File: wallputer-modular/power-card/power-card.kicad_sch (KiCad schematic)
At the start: 1 part

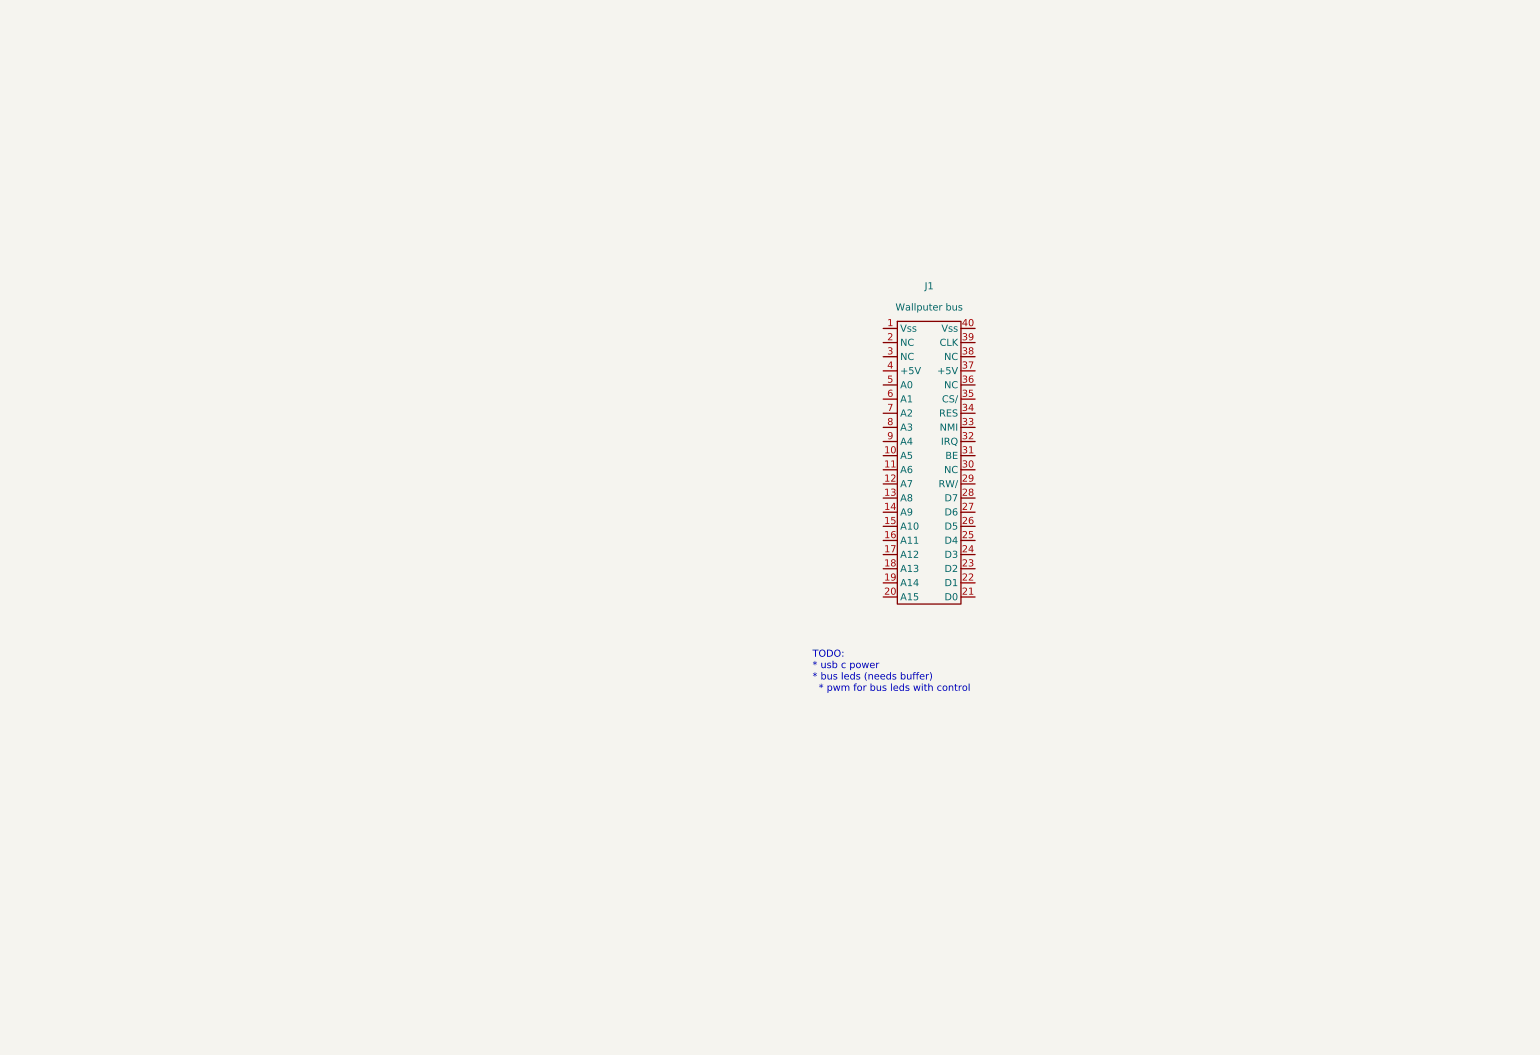
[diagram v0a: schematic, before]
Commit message: implement power module
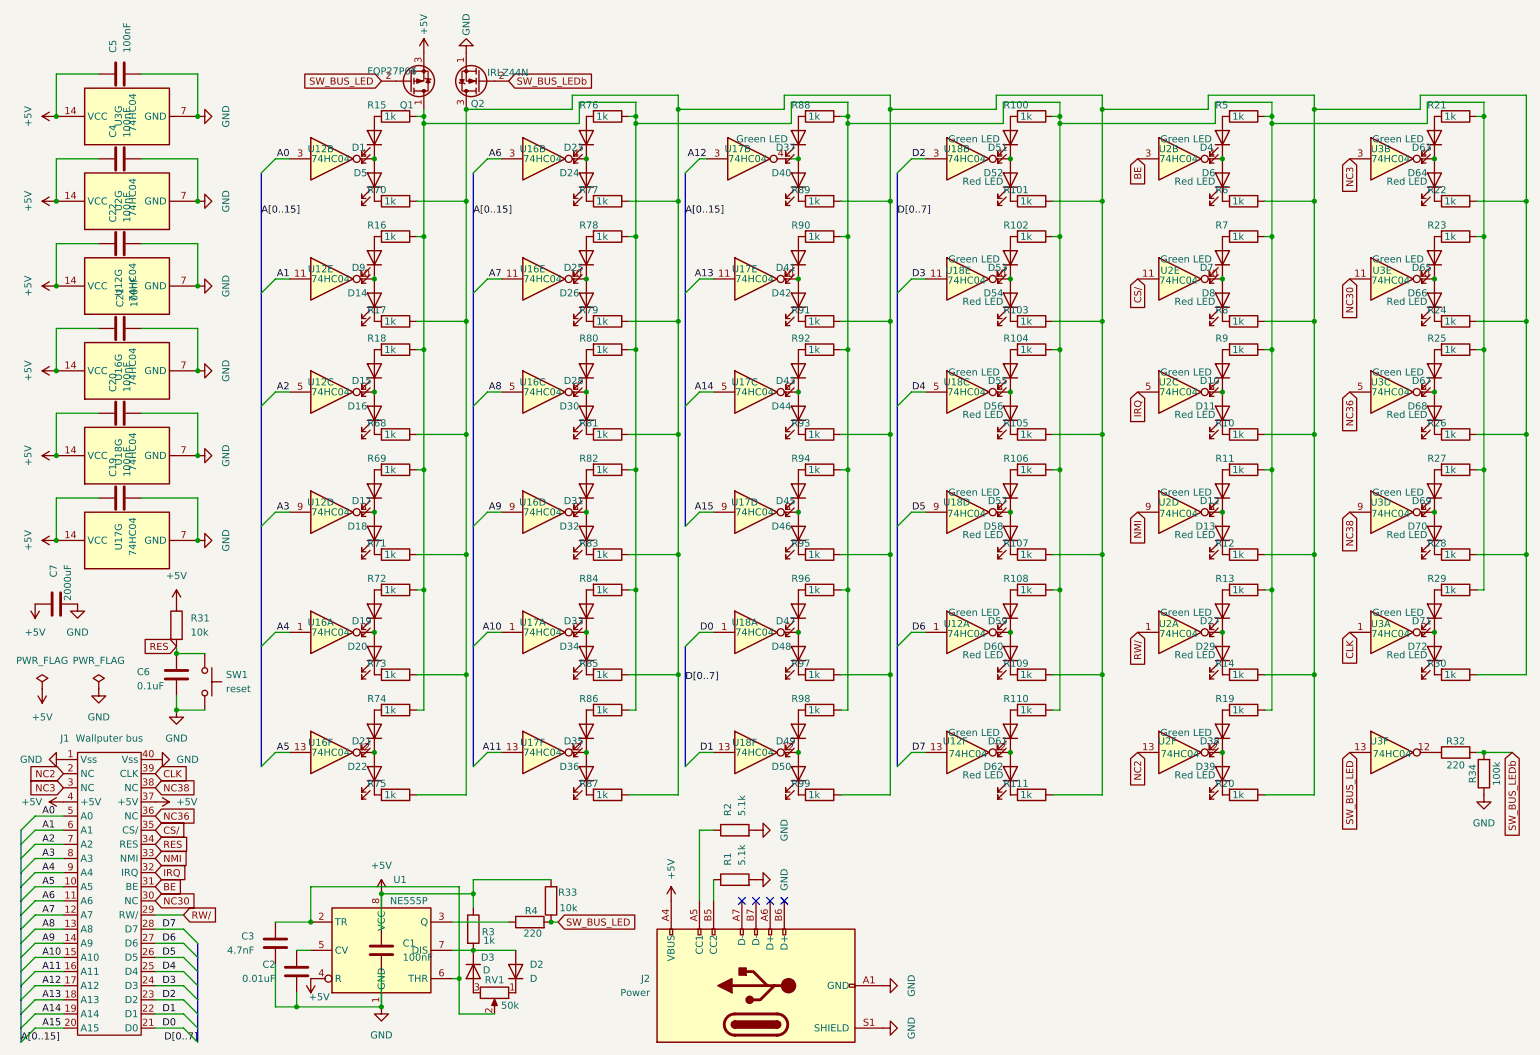
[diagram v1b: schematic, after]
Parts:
- added C1: 100nF, symbol Device:C
- added C19, C20, C21, C22, C4, C5: 100nF, Capacitor_THT:C_Disc_D5.0mm_W2.5mm_P5.00mm, symbol Device:C
- added C2: 0.01uF, symbol Device:C
- added C3: 4.7nF, symbol Device:C
- added C6: 0.1uF, symbol Device:C
- added C7: 2000uF, symbol Device:C
- added D1, D10, D12, D15, D17, D19, D21, D23, D25, D27, D28, D31, D33, D35, D37, D38, D4, D41, D43, D45, D47, D49, D51, D53, D55, D57, D59, D61, D63, D65, D67, D69, D7, D71, D9: Green LED, LED_THT:LED_D3.0mm, symbol Device:LED
- added D11, D13, D14, D16, D18, D20, D22, D24, D26, D29, D30, D32, D34, D36, D39, D40, D42, D44, D46, D48, D5, D50, D52, D54, D56, D58, D6, D60, D62, D64, D66, D68, D70, D72, D8: Red LED, LED_THT:LED_D3.0mm, symbol Device:LED
- added D2, D3: D, symbol Device:D
- added J2: Power, symbol Connector:USB_C_Receptacle_USB2.0_14P
- added Q1: FQP27P06, Package_TO_SOT_THT:TO-92_Inline, symbol Transistor_FET:BS250
- added Q2: IRLZ44N, Package_TO_SOT_THT:TO-92_Inline, symbol Transistor_FET:2N7000
- added R1, R2: 5.1k, symbol Device:R
- added R10, R100, R101, R102, R103, R104, R105, R106, R107, R108, R109, R11, R110, R111, R12, R13, R14, R15, R16, R17, R18, R19, R20, R21, R22, R23, R24, R25, R26, R27, R28, R29, R30, R5, R6, R68, R69, R7, R70, R71, R72, R73, R74, R75, R76, R77, R78, R79, R8, R80, R81, R82, R83, R84, R85, R86, R87, R88, R89, R9, R90, R91, R92, R93, R94, R95, R96, R97, R98, R99: 1k, Resistor_THT:R_Axial_DIN0204_L3.6mm_D1.6mm_P2.54mm_Vertical, symbol Device:R
- added R3: 1k, symbol Device:R
- added R31, R33: 10k, symbol Device:R
- added R32, R4: 220, symbol Device:R
- added R34: 100k, symbol Device:R
- added RV1: 50k, symbol Device:R_Potentiometer
- added SW1: reset, symbol Switch:SW_Push
- added U1: NE555P, Package_DIP:DIP-8_W7.62mm, symbol Timer:NE555P
- added U12, U16, U17, U18, U2, U3: 74HC04, Package_DIP:DIP-14_W7.62mm_Socket, symbol 74xx:74HC04
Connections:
- net GND: now reaches J1.1 (Vss)
- net GND: now also J1.40 (Vss), C1.2, C19.2, C2.1, C20.2, C21.2, C22.2, C3.2, C4.2, C5.2, C6.2, C7.2, J2.A1 (GND), J2.A12 (GND), J2.B1 (GND), J2.B12 (GND), J2.S1 (SHIELD), Q2.1 (S), R1.2, R2.2, R34.1, SW1.2, U1.1 (GND), U12.7 (GND), U16.7 (GND), U17.7 (GND), U18.7 (GND), U2.7 (GND), U3.7 (GND)
- net A5: now reaches J1.10 (A5)
- net A5: now also U16.13
- net A6: now reaches J1.11 (A6)
- net A6: now also U16.3
- net A7: now reaches J1.12 (A7)
- net A7: now also U16.11
- net A8: now reaches J1.13 (A8)
- net A8: now also U16.5
- net A9: now reaches J1.14 (A9)
- net A9: now also U16.9
- net A10: now reaches J1.15 (A10)
- net A10: now also U17.1
- net A11: now reaches J1.16 (A11)
- net A11: now also U17.13
- net A12: now reaches J1.17 (A12)
- net A12: now also U17.3
- net A13: now reaches J1.18 (A13)
- net A13: now also U17.11
- net A14: now reaches J1.19 (A14)
- net A14: now also U17.5
- net NC2: now reaches J1.2 (NC)
- net NC2: now also U2.13
- net A15: now reaches J1.20 (A15)
- net A15: now also U17.9
- net D0: now reaches J1.21 (D0)
- net D0: now also U18.1
- net D1: now reaches J1.22 (D1)
- net D1: now also U18.13
- net D2: now reaches J1.23 (D2)
- net D2: now also U18.3
- net D3: now reaches J1.24 (D3)
- net D3: now also U18.11
- net D4: now reaches J1.25 (D4)
- net D4: now also U18.5
- net D5: now reaches J1.26 (D5)
- net D5: now also U18.9
- net D6: now reaches J1.27 (D6)
- net D6: now also U12.1
- net D7: now reaches J1.28 (D7)
- net D7: now also U12.13
- net RW/: now reaches J1.29 (RW/)
- net RW/: now also U2.1
- net NC3: now reaches J1.3 (NC)
- net NC3: now also U3.3
- net NC30: now reaches J1.30 (NC)
- net NC30: now also U3.11
- net BE: now reaches J1.31 (BE)
- net BE: now also U2.3
- net IRQ: now reaches J1.32 (IRQ)
- net IRQ: now also U2.5
- net NMI: now reaches J1.33 (NMI)
- net NMI: now also U2.9
- net RES: now reaches J1.34 (RES)
- net RES: now also C6.1, R31.2, SW1.1
- net CS/: now reaches J1.35 (CS/)
- net CS/: now also U2.11
- net NC36: now reaches J1.36 (NC)
- net NC36: now also U3.5
- net +5V: now reaches J1.37 (+5V)
- net +5V: now also J1.4 (+5V), C1.1, C19.1, C20.1, C21.1, C22.1, C4.1, C5.1, C7.1, J2.A4 (VBUS), J2.A9 (VBUS), J2.B4 (VBUS), J2.B9 (VBUS), Q1.3 (S), R3.1, R31.1, R33.2, U1.4 (R), U1.8 (VCC), U12.14 (VCC), U16.14 (VCC), U17.14 (VCC), U18.14 (VCC), U2.14 (VCC), U3.14 (VCC)
- net NC38: now reaches J1.38 (NC)
- net NC38: now also U3.9
- net CLK: now reaches J1.39 (CLK)
- net CLK: now also U3.1
- net A0: now reaches J1.5 (A0)
- net A0: now also U12.3
- net A1: now reaches J1.6 (A1)
- net A1: now also U12.11
- net A2: now reaches J1.7 (A2)
- net A2: now also U12.5
- net A3: now reaches J1.8 (A3)
- net A3: now also U12.9
- net A4: now reaches J1.9 (A4)
- net A4: now also U16.1
- new net: D26.1 (K), R79.2
- new net: D25.1 (K), D26.2 (A), U16.10
- new net: D35.1 (K), D36.2 (A), U17.12
- new net: J2.B5 (CC2), R1.1
- new net: C3.1, RV1.2, U1.2 (TR), U1.6 (THR)
- new net: D1.1 (K), D5.2 (A), U12.4
- new net: D14.2 (A), D9.1 (K), U12.10
- new net: D9.2 (A), R16.2
- new net: D63.1 (K), D64.2 (A), U3.4
- new net: D63.2 (A), R21.2
- new net: D8.1 (K), R8.2
- new net: D7.1 (K), D8.2 (A), U2.10
- new net: Q2.3 (D), R10.1, R101.1, R103.1, R105.1, R107.1, R109.1, R111.1, R12.1, R14.1, R17.1, R20.1, R22.1, R24.1, R26.1, R28.1, R30.1, R6.1, R68.1, R70.1, R71.1, R73.1, R75.1, R77.1, R79.1, R8.1, R81.1, R83.1, R85.1, R87.1, R89.1, R91.1, R93.1, R95.1, R97.1, R99.1
- new net: D62.1 (K), R111.2
- new net: D37.1 (K), D40.2 (A), U17.4
- new net: D64.1 (K), R22.2
- new net: Q1.1 (D), R100.1, R102.1, R104.1, R106.1, R108.1, R11.1, R110.1, R13.1, R15.1, R16.1, R18.1, R19.1, R21.1, R23.1, R25.1, R27.1, R29.1, R5.1, R69.1, R7.1, R72.1, R74.1, R76.1, R78.1, R80.1, R82.1, R84.1, R86.1, R88.1, R9.1, R90.1, R92.1, R94.1, R96.1, R98.1
- new net: D43.2 (A), R92.2
- new net: D16.1 (K), R68.2
- new net: D15.1 (K), D16.2 (A), U12.6
- new net: D49.2 (A), R98.2
- new net: D39.1 (K), R20.2
- new net: D38.1 (K), D39.2 (A), U2.12
- new net: J2.A5 (CC1), R2.1
- new net: D44.1 (K), R93.2
- new net: D43.1 (K), D44.2 (A), U17.6
- new net: D1.2 (A), R15.2
- new net: D33.2 (A), R84.2
- new net: D27.1 (K), D29.2 (A), U2.2
- new net: D47.1 (K), D48.2 (A), U18.2
- new net: D47.2 (A), R96.2
- new net: D41.1 (K), D42.2 (A), U17.10
- new net: D41.2 (A), R90.2
- new net: D24.1 (K), R77.2
- new net: D23.1 (K), D24.2 (A), U16.4
- new net: D56.1 (K), R105.2
- new net: D55.1 (K), D56.2 (A), U18.6
- new net: D23.2 (A), R76.2
- new net: D32.1 (K), R83.2
- new net: R32.1, U3.12
- new net: D27.2 (A), R13.2
- new net: D25.2 (A), R78.2
- new net: D31.1 (K), D32.2 (A), U16.8
- new net: D31.2 (A), R82.2
- new net: D22.1 (K), R75.2
- new net: D12.1 (K), D13.2 (A), U2.8
- new net: D12.2 (A), R11.2
- new net: D65.1 (K), D66.2 (A), U3.10
- new net: D65.2 (A), R23.2
- new net: D52.1 (K), R101.2
- new net: D51.1 (K), D52.2 (A), U18.4
- new net: D2.2 (A), D3.1 (K), R3.2, U1.7 (DIS)
- new net: D3.2 (A), RV1.3
- new net: D40.1 (K), R89.2
- new net: D46.1 (K), R95.2
- new net: D13.1 (K), R12.2
- new net: D18.1 (K), R71.2
- new net: D17.1 (K), D18.2 (A), U12.8
- new net: D60.1 (K), R109.2
- new net: D59.1 (K), D60.2 (A), U12.2
- new net: D53.1 (K), D54.2 (A), U18.10
- new net: D36.1 (K), R87.2
- new net: D21.2 (A), R74.2
- new net: D50.1 (K), R99.2
- new net: D49.1 (K), D50.2 (A), U18.12
- new net: D17.2 (A), R69.2
- new net: D42.1 (K), R91.2
- new net: D29.1 (K), R14.2
- new net: D28.1 (K), D30.2 (A), U16.6
- new net: D72.1 (K), R30.2
- new net: D71.1 (K), D72.2 (A), U3.2
- new net: D66.1 (K), R24.2
- new net: D21.1 (K), D22.2 (A), U16.12
- new net: D15.2 (A), R18.2
- new net: D5.1 (K), R70.2
- new net: D48.1 (K), R97.2
- new net: D51.2 (A), R100.2
- new net: D53.2 (A), R102.2
- new net: D34.1 (K), R85.2
- new net: D33.1 (K), D34.2 (A), U17.2
- new net: D10.1 (K), D11.2 (A), U2.6
- new net: D10.2 (A), R9.2
- new net: D38.2 (A), R19.2
- new net: D59.2 (A), R108.2
- new net: D57.1 (K), D58.2 (A), U18.8
- new net: D37.2 (A), R88.2
- new net: D20.1 (K), R73.2
- new net: D19.1 (K), D20.2 (A), U16.2
- new net: D30.1 (K), R81.2
- new net: D68.1 (K), R26.2
- new net: D45.1 (K), D46.2 (A), U17.8
- new net: D57.2 (A), R106.2
- new net: D61.1 (K), D62.2 (A), U12.12
- new net: D61.2 (A), R110.2
- new net: D71.2 (A), R29.2
- new net: D35.2 (A), R86.2
- new net: D14.1 (K), R17.2
- new net: D67.1 (K), D68.2 (A), U3.6
- new net: D67.2 (A), R25.2
- new net: C2.2, U1.5 (CV)
- new net: D6.1 (K), R6.2
- new net: D4.1 (K), D6.2 (A), U2.4
- new net: D69.1 (K), D70.2 (A), U3.8
- new net: D69.2 (A), R27.2
- new net: R4.1, U1.3 (Q)
- new net: D70.1 (K), R28.2
- new net: D4.2 (A), R5.2
- new net: D45.2 (A), R94.2
- new net: D58.1 (K), R107.2
- new net: D55.2 (A), R104.2
- new net: D28.2 (A), R80.2
- new net: D54.1 (K), R103.2
- new net: D2.1 (K), RV1.1
- new net: D7.2 (A), R7.2
- new net: D19.2 (A), R72.2
- new net: D11.1 (K), R10.2
- new net SW_BUS_LED: Q1.2 (G), R33.1, R4.2, U3.13
- new net SW_BUS_LEDb: Q2.2 (G), R32.2, R34.2
- no-connect marks 0 -> 4
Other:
- note removed: "TODO: * usb c power * bus leds (needs buffer) * pwm for bus leds with control"

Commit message: fix errors
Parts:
- removed C7: 2000uF, symbol Device:C
- added C7: 2000uF, Capacitor_THT:CP_Radial_D18.0mm_P7.50mm, symbol Device:C_Polarized
- Q1: footprint Package_TO_SOT_THT:TO-92_Inline -> Package_TO_SOT_THT:TO-220-3_Vertical; symbol Transistor_FET:BS250 -> Transistor_FET:FQP27P06
- Q2: footprint Package_TO_SOT_THT:TO-92_Inline -> Package_TO_SOT_THT:TO-220-3_Vertical; symbol Transistor_FET:2N7000 -> Transistor_FET:IRLZ44N
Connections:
- net +5V: now also C7.1
- net GND: now also Q2.3 (S), C7.2; no longer Q2.1 (S)
- net SW_BUS_LED: now also Q1.1 (G); no longer Q1.2 (G)
- net SW_BUS_LEDb: now also Q2.1 (G); no longer Q2.2 (G)
- net at R10.1, R101.1, R103.1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: now also Q2.2 (D); no longer Q2.3 (D)
- net at R100.1, R102.1, R104.1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: now also Q1.2 (D); no longer Q1.1 (D)
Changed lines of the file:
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@@
 	)
 	(symbol
-		(lib_id "Transistor_FET:BS250")
+		(lib_id "Transistor_FET:FQP27P06")
 		(at 82.55 24.13 0)
 		(mirror x)
@@
 			)
 		)
-		(property "Footprint" "Package_TO_SOT_THT:TO-92_Inline"
+		(property "Footprint" "Package_TO_SOT_THT:TO-220-3_Vertical"
 			(at 87.63 22.225 0)
 			(effects
@@
 			)
 		)
-		(property "Datasheet" "http://www.vishay.com/docs/70209/70209.pdf"
+		(property "Datasheet" "https://www.onsemi.com/pub/Collateral/FQP27P06-D.PDF"
 			(at 87.63 20.32 0)
 			(effects
@@
 			)
 		)
-		(property "Description" "-0.18A Id, -45V Vds, P-Channel MOSFET, TO-92"
+		(property "Description" "-27A Id, -60V Vds, QFET P-Channel MOSFET, TO-220"
 			(at 82.55 24.13 0)
 			(effects
@@
 	)
 	(symbol
-		(lib_id "Device:C")
-		(at 19.05 118.11 90)
-		(mirror x)
-		(unit 1)
-		(exclude_from_sim no)
-		(in_bom yes)
-		(on_board yes)
-		(dnp no)
-		(property "Reference" "C7"
-			(at 18.542 110.998 0)
-			(effects
-				(font
-					(size 1.27 1.27)
-				)
-				(justify left)
-			)
-		)
-		(property "Value" "2000uF"
-			(at 21.082 110.998 0)
-			(effects
-				(font
-					(size 1.27 1.27)
-				)
-				(justify left)
-			)
-		)
-		(property "Footprint" ""
-			(at 22.86 119.0752 0)
-			(effects
-				(font
-					(size 1.27 1.27)
-				)
-				(hide yes)
-			)
-		)
-		(property "Datasheet" "~"
-			(at 19.05 118.11 0)
-			(effects
-				(font
-					(size 1.27 1.27)
-				)
-				(hide yes)
-			)
-		)
-		(property "Description" "Unpolarized capacitor"
-			(at 19.05 118.11 0)
-			(effects
-				(font
-					(size 1.27 1.27)
-				)
-				(hide yes)
-			)
-		)
-		(pin "1"
-		)
-		(pin "2"
-		)
-		(instances
-			(project "power-card"
-				(path "/27eadfe8-fd7c-478e-bb9f-863e2465d9f9"
-					(reference "C7")
-					(unit 1)
-				)
-			)
-		)
-	)
-	(symbol
 		(lib_id "74xx:74HC04")
 		(at 68.58 101.6 0)
@@
 	)
 	(symbol
-		(lib_id "Transistor_FET:2N7000")
+		(lib_id "Transistor_FET:IRLZ44N")
 		(at 95.25 24.13 180)
 		(unit 1)
@@
 			)
 		)
-		(property "Footprint" "Package_TO_SOT_THT:TO-92_Inline"
+		(property "Footprint" "Package_TO_SOT_THT:TO-220-3_Vertical"
 			(at 90.17 22.225 0)
 			(effects
@@
 			)
 		)
-		(property "Datasheet" "https://www.vishay.com/docs/70226/70226.pdf"
+		(property "Datasheet" "http://www.irf.com/product-info/datasheets/data/irlz44n.pdf"
 			(at 90.17 20.32 0)
 			(effects
@@
 			)
 		)
-		(property "Description" "0.2A Id, 200V Vds, N-Channel MOSFET, 2.6V Logic Level, TO-92"
+		(property "Description" "47A Id, 55V Vds, 22mOhm Rds Single N-Channel HEXFET Power MOSFET, TO-220AB"
 			(at 95.25 24.13 0)
 			(effects
@@
 					(unit 1)
 				)
+			)
+		)
+	)
+	(symbol
+		(lib_id "Device:C_Polarized")
+		(at 19.05 118.11 90)
+		(unit 1)
+		(exclude_from_sim no)
+		(in_bom yes)
+		(on_board yes)
+		(dnp no)
+		(property "Reference" "C7"
+			(at 16.256 116.84 90)
+			(effects
+				(font
+					(size 1.27 1.27)
+				)
+			)
+		)
+		(property "Value" "2000uF"
+			(at 24.13 116.84 90)
+			(effects
+				(font
+					(size 1.27 1.27)
+				)
+			)
+		)
+		(property "Footprint" "Capacitor_THT:CP_Radial_D18.0mm_P7.50mm"
+			(at 22.86 117.1448 0)
+			(effects
+				(font
+					(size 1.27 1.27)
+				)
+				(hide yes)
+			)
+		)
+		(property "Datasheet" "~"
+			(at 19.05 118.11 0)
+			(effects
+				(font
+					(size 1.27 1.27)
+				)
+				(hide yes)
+			)
+		)
+		(property "Description" "Polarized capacitor"
+			(at 19.05 118.11 0)
+			(effects
+				(font
+					(size 1.27 1.27)
+				)
+				(hide yes)
+			)
+		)
+		(pin "2"
+		)
+		(pin "1"
+		)
+		(instances
+			(project ""
+				(path "/27eadfe8-fd7c-478e-bb9f-863e2465d9f9"
+					(reference "C7")
+					(unit 1)
+				)

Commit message: footprints
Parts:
- C1, C2, C3, C6: footprint (none) -> Capacitor_THT:C_Disc_D5.0mm_W2.5mm_P5.00mm
- D2, D3: value D -> 1n4148; footprint (none) -> Diode_THT:D_DO-35_SOD27_P7.62mm_Horizontal
- J2: footprint (none) -> Connector_USB:USB_C_Receptacle_HRO_TYPE-C-31-M-12
- R1, R2, R3, R31, R32, R33, R34, R4: footprint (none) -> Resistor_THT:R_Axial_DIN0204_L3.6mm_D1.6mm_P2.54mm_Vertical
- RV1: footprint (none) -> Potentiometer_THT:Potentiometer_Alpha_RD901F-40-00D_Single_Vertical
- SW1: footprint (none) -> Button_Switch_THT:SW_PUSH_6mm_H4.3mm
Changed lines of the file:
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@@
 			)
 		)
-		(property "Footprint" ""
+		(property "Footprint" "Resistor_THT:R_Axial_DIN0204_L3.6mm_D1.6mm_P2.54mm_Vertical"
 			(at 140.97 169.418 90)
 			(effects
@@
 			)
 		)
-		(property "Footprint" ""
+		(property "Footprint" "Capacitor_THT:C_Disc_D5.0mm_W2.5mm_P5.00mm"
 			(at 57.4548 182.88 0)
 			(effects
@@
 			)
 		)
-		(property "Footprint" ""
+		(property "Footprint" "Resistor_THT:R_Axial_DIN0204_L3.6mm_D1.6mm_P2.54mm_Vertical"
 			(at 140.97 160.528 90)
 			(effects
@@
 			)
 		)
-		(property "Footprint" ""
+		(property "Footprint" "Connector_USB:USB_C_Receptacle_HRO_TYPE-C-31-M-12"
 			(at 144.78 182.88 0)
 			(effects
@@
 			)
 		)
-		(property "Value" "D"
+		(property "Value" "1n4148"
 			(at 97.028 183.896 90)
 			(effects
@@
 			)
 		)
-		(property "Footprint" ""
+		(property "Footprint" "Diode_THT:D_DO-35_SOD27_P7.62mm_Horizontal"
 			(at 93.98 184.15 0)
 			(effects
@@
 			)
 		)
-		(property "Footprint" ""
+		(property "Footprint" "Resistor_THT:R_Axial_DIN0204_L3.6mm_D1.6mm_P2.54mm_Vertical"
 			(at 270.51 146.558 90)
 			(effects
@@
 			)
 		)
-		(property "Footprint" ""
+		(property "Footprint" "Resistor_THT:R_Axial_DIN0204_L3.6mm_D1.6mm_P2.54mm_Vertical"
 			(at 38.862 121.92 90)
 			(effects
@@
 			)
 		)
-		(property "Footprint" ""
+		(property "Footprint" "Capacitor_THT:C_Disc_D5.0mm_W2.5mm_P5.00mm"
 			(at 78.4352 184.15 0)
 			(effects
@@
 			)
 		)
-		(property "Footprint" ""
+		(property "Footprint" "Resistor_THT:R_Axial_DIN0204_L3.6mm_D1.6mm_P2.54mm_Vertical"
 			(at 277.368 148.59 90)
 			(effects
@@
 			)
 		)
-		(property "Footprint" ""
+		(property "Footprint" "Capacitor_THT:C_Disc_D5.0mm_W2.5mm_P5.00mm"
 			(at 63.1952 180.34 0)
 			(effects
@@
 			)
 		)
-		(property "Footprint" ""
+		(property "Footprint" "Resistor_THT:R_Axial_DIN0204_L3.6mm_D1.6mm_P2.54mm_Vertical"
 			(at 104.14 177.038 90)
 			(effects
@@
 			)
 		)
-		(property "Value" "D"
+		(property "Value" "1n4148"
 			(at 104.14 185.4199 90)
 			(effects
@@
 			)
 		)
-		(property "Footprint" ""
+		(property "Footprint" "Diode_THT:D_DO-35_SOD27_P7.62mm_Horizontal"
 			(at 101.6 184.15 0)
 			(effects
@@
 			)
 		)
-		(property "Footprint" ""
+		(property "Footprint" "Potentiometer_THT:Potentiometer_Alpha_RD901F-40-00D_Single_Vertical"
 			(at 97.79 187.96 0)
 			(effects
@@
 			)
 		)
-		(property "Footprint" ""
+		(property "Footprint" "Capacitor_THT:C_Disc_D5.0mm_W2.5mm_P5.00mm"
 			(at 41.6052 134.62 0)
 			(effects
@@
 			)
 		)
-		(property "Footprint" ""
+		(property "Footprint" "Resistor_THT:R_Axial_DIN0204_L3.6mm_D1.6mm_P2.54mm_Vertical"
 			(at 109.728 171.45 90)
 			(effects
@@
 			)
 		)
-		(property "Footprint" ""
+		(property "Footprint" "Resistor_THT:R_Axial_DIN0204_L3.6mm_D1.6mm_P2.54mm_Vertical"
 			(at 92.202 176.53 90)
 			(effects
@@
 			)
 		)
-		(property "Footprint" ""
+		(property "Footprint" "Button_Switch_THT:SW_PUSH_6mm_H4.3mm"
 			(at 50.8 132.08 0)
 			(effects
